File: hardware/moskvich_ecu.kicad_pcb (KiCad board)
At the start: 2 copper layers, 101.6 x 63.5 mm, 44 parts, among them J1 Power, J2 Sensors, Q1 ISL9V3040P3, Q2 BC547B, U1 ESP32-C3-Zero, U2 TSR 1-2450, U3 74HCT123N

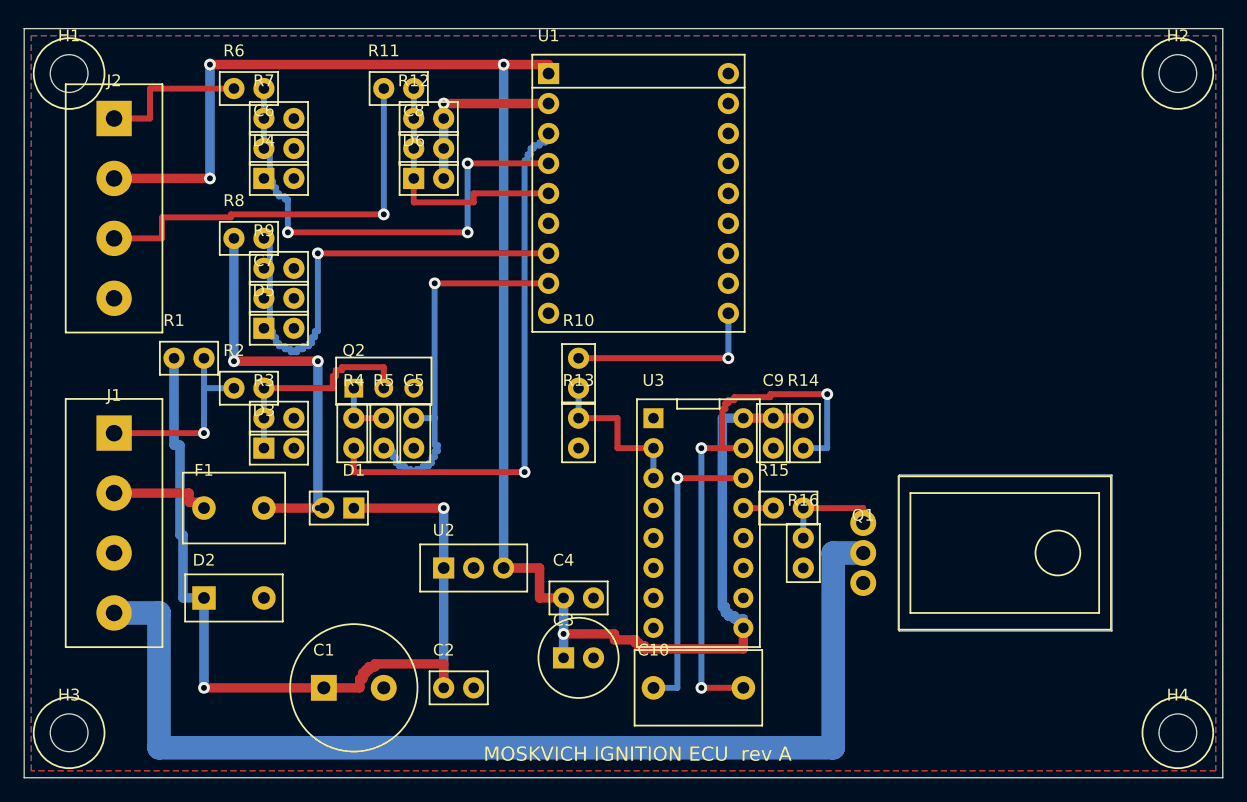
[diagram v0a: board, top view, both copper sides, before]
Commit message: Hardware rev B: SMD two-sided board (48 x 41.8 mm), AP63205 SMD buck, SOIC/SOT parts, 3.5 mm terminals, IGBT cut-out
Co-Authored-By: Claude Sonnet 5.5 <noreply@anthropic.com>
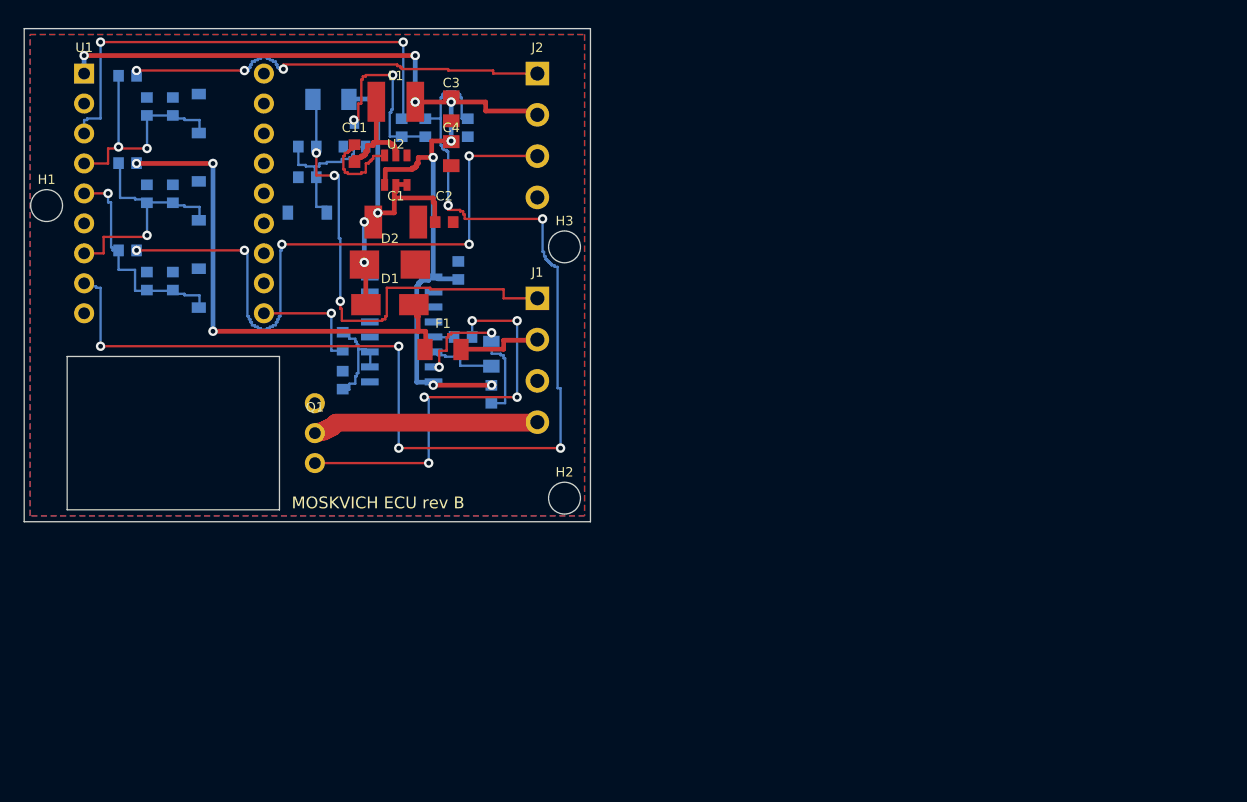
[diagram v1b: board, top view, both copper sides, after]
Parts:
- removed H4: M3, MountingHole_3.2
- added C11: 100nF, C_0603, F.Cu at (28.0, 10.6)
- added L1: 4.7uH, L_4x4, F.Cu at (31.5, 6.20)
- C1: value 470uF 35V -> 10uF 50V; footprint CP_Radial_D10_P5.08 -> C_1210
- C10: value 1uF film -> 2.2uF 25V X7R; footprint C_Rect_P7.62 -> C_0805; moved to B.Cu
- C2: footprint C_Disc_P2.54 -> C_0603
- C3: value 100uF 16V -> 22uF 10V; footprint CP_Radial_D6.3_P2.54 -> C_0805
- C4: value 100nF -> 22uF 10V; footprint C_Disc_P2.54 -> C_0805
- C5, C6, C7, C8, C9: footprint C_Disc_P2.54 -> C_0603; moved to B.Cu
- D1: value 1N5819 -> SS34; footprint D_Axial_Vertical_P2.54 -> D_SMA
- D2: value P6KE27A -> SMBJ24A; footprint D_DO-15_Vertical_P5.08 -> D_SMB
- D3: value 1N4148 -> 1N4148W; footprint D_Axial_Vertical_P2.54 -> D_SOD-123; moved to B.Cu
- D4, D5, D6: value BZX55C3V6 -> BZT52C3V6; footprint D_Axial_Vertical_P2.54 -> D_SOD-123; moved to B.Cu
- F1: value 500mA PTC -> 0.5A 32V fuse; footprint Fuse_Radial_P5.08 -> Fuse_1206
- H1, H2, H3: value M3 -> M2.5; footprint MountingHole_3.2 -> MountingHole_2.7_M2.5
- J1, J2: footprint TerminalBlock_P5.08_1x04 -> TerminalBlock_P3.50_1x04
- Q2: value BC547B -> BC847B; footprint TO-92_Inline -> SOT-23; moved to B.Cu
- R1: value 1k 0.5W -> 1k 0.25W; footprint R_Axial_Vertical_P2.54 -> R_1206; moved to B.Cu
- R10, R11, R12, R13, R15, R16, R2, R3, R4, R5, R6, R7, R8, R9: footprint R_Axial_Vertical_P2.54 -> R_0603; moved to B.Cu
- R14: value 27k -> 22k; footprint R_Axial_Vertical_P2.54 -> R_0603; moved to B.Cu
- U2: value TSR 1-2450 -> AP63205WU-7; footprint SIP3_TSR1 -> SOT-23-6
- U3: value 74HCT123N -> SN74HCT123D; footprint DIP-16_W7.62 -> SOIC-16_3.9x9.9mm_P1.27mm; moved to B.Cu
- moved H2 63.2 mm to (45.8, 39.8)
- moved H3 58.8 mm to (45.8, 18.5)
- moved Q1 47.6 mm to (24.6, 34.3)
- moved C3 47.5 mm to (36.2, 6.80)
- moved C1 39.9 mm to (31.5, 16.4)
- moved C2 39.5 mm to (35.6, 16.4)
- moved U1 39.4 mm to (5.08, 3.81)
- moved C4 38.8 mm to (36.2, 10.6)
- moved J1 37.7 mm to (43.5, 22.9)
- moved J2 36.1 mm to (43.5, 3.81)
- moved U2 34.0 mm to (31.5, 12.0)
- moved R16 33.9 mm to (33.5, 33.5)
- moved D2 32.4 mm to (31.0, 20.0)
- moved C10 31.4 mm to (39.6, 27.6)
- moved R15 30.0 mm to (37.2, 26.1)
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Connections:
- C5 pad 1: PT_G -> GND
- C5 pad 2: GND -> PT_G
- F1 pad 1: +12V_IN -> VBAT_F
- F1 pad 2: VBAT_F -> +12V_IN
- Q2 pad 1: PT_C -> PT_B
- Q2 pad 2: PT_B -> GND
- Q2 pad 3: GND -> PT_C
- R14 pad 1: +5V -> REXT
- R14 pad 2: REXT -> +5V
- R15 pad 1: GATE_DRV -> GATE
- R15 pad 2: GATE -> GATE_DRV
- U2 pad 1: VIN_P -> +5V
- U2 pad 2: GND -> VIN_P
- U2 pad 3: +5V -> VIN_P
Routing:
- net COIL_N: track 91.4 -> 19.8 mm
- net PT_G: track 34.3 -> 100.6 mm, vias 1 -> 6
- net +5V: track 147.3 -> 88.0 mm, vias 4 -> 8
- net VIN_P: track 77.7 -> 31.8 mm, vias 2 -> 3
- net REXT: track 47.5 -> 16.2 mm, vias 3 -> 2
- net GATE: track 8.89 -> 35.2 mm, vias 0 -> 5
- net POINTS_RAW: track 16.5 -> 41.6 mm, vias 1 -> 3
- net LPG_IN: track 12.7 -> 37.8 mm, vias 0 -> 3
- net VB_S: track 43.7 -> 21.5 mm
- net LPG_S: track 42.7 -> 21.8 mm, vias 3 -> 2
- net MAP_SIG: track 35.6 -> 55.5 mm, vias 1 -> 5
- net CEXT: track 25.4 -> 6.14 mm, vias 1 -> 0
- net GND: track 15.2 -> 0.00 mm, vias 1 -> 0
- net PT_C: track 5.08 -> 15.9 mm, vias 0 -> 2
- net SW: track 0.00 -> 9.89 mm
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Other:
- board size 101.6 x 63.5 mm -> 48 x 41.8 mm
- board text added: "MOSKVICH ECU rev B"
- board text removed: "MOSKVICH IGNITION ECU rev A"

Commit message: hardware: switch the coil guard to CD74HCT221M96 (same pinout, tW = 0.7 R C), R14 = 15k
Co-Authored-By: Claude Sonnet 5.5 <noreply@anthropic.com>
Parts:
- R14: value 22k -> 15k
- U3: value SN74HCT123D -> CD74HCT221M96
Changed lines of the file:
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@@
   )
   (footprint "SOIC-16_3.9x9.9mm_P1.27mm" (layer "B.Cu") (at 32.000 25.500)
-    (descr "retriggerable one-shot = coil on-time guard + 5 V gate driver")
+    (descr "monostable = coil on-time guard + 5 V gate driver")
     (fp_text reference "U3" (at 0 -2.2) (layer "B.SilkS") (effects (font (size 0.8 0.8) (thickness 0.12)) (justify mirror)))
-    (fp_text value "SN74HCT123D" (at 0 2.2) (layer "B.Fab") (effects (font (size 0.8 0.8) (thickness 0.12)) (justify mirror)))
+    (fp_text value "CD74HCT221M96" (at 0 2.2) (layer "B.Fab") (effects (font (size 0.8 0.8) (thickness 0.12)) (justify mirror)))
     (pad "1" smd rect (at -2.700 4.445) (size 1.5 0.6) (layers "B.Cu" "B.Paste" "B.Mask") (net 1 "GND"))
     (pad "2" smd rect (at -2.700 3.175) (size 1.5 0.6) (layers "B.Cu" "B.Paste" "B.Mask") (net 20 "CMD"))
@@
   )
   (footprint "R_0603" (layer "B.Cu") (at 39.600 31.000)
-    (descr "22k")
+    (descr "15k")
     (fp_text reference "R14" (at 0 -2.2) (layer "B.SilkS") (effects (font (size 0.8 0.8) (thickness 0.12)) (justify mirror)))
-    (fp_text value "22k" (at 0 2.2) (layer "B.Fab") (effects (font (size 0.8 0.8) (thickness 0.12)) (justify mirror)))
+    (fp_text value "15k" (at 0 2.2) (layer "B.Fab") (effects (font (size 0.8 0.8) (thickness 0.12)) (justify mirror)))
     (pad "1" smd rect (at 0.000 0.762) (size 1.0 0.9) (layers "B.Cu" "B.Paste" "B.Mask") (net 24 "REXT"))
     (pad "2" smd rect (at 0.000 -0.762) (size 1.0 0.9) (layers "B.Cu" "B.Paste" "B.Mask") (net 2 "+5V"))
